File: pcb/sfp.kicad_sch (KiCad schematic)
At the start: 5 parts, among them J1 SFP, U1 GW1N-6&9_QN48

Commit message: pcb: schemat rev. A
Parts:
- added C10, C12, C8: 100n, Capacitor_SMD:C_0603_1608Metric, symbol Device:C
- added C11, C9: 10u, Capacitor_SMD:C_0603_1608Metric, symbol Device:C
- added D2, D3: LED, LED_SMD:LED_0603_1608Metric, symbol Device:LED
- added L1, L2: 1uH, Inductor_SMD:L_0805_2012Metric, symbol Device:L
- added R10, R9: 49.9 1%, Resistor_SMD:R_0402_1005Metric, symbol Device:R
- added R11: 2.1k, Resistor_SMD:R_0603_1608Metric, symbol Device:R
- added R12: 1.2k, Resistor_SMD:R_0603_1608Metric, symbol Device:R
- added R14, R15: 1k, Resistor_SMD:R_0603_1608Metric, symbol Device:R
- added Y1: OT322525MJBA4SL, Oscillator:Oscillator_SMD_Abracon_ASE-4Pin_3.2x2.5mm, symbol Oscillator:ASE-xxxMHz
- C6, C7: footprint Capacitor_SMD:C_0402_1005Metric -> Capacitor_SMD:C_0603_1608Metric
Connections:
- net RD+ is gone; now on net SFP_RD_P: J1.13 (RD+)
- net RD- is gone; now on net SFP_RD_N: J1.12 (RD-)
- net TD+ is gone; now on net SFP_TD_P: J1.18 (TD+)
- net TD- is gone; now on net SFP_TD_N: J1.19 (TD-)
- net CLK_25M: now also Y1.3 (OUT)
- net GND: now also C6.2, C7.2, C10.2, C11.2, C12.2, C8.2, C9.2, R12.2, Y1.2 (GND)
- net LED_ACT: now also D3.1 (K)
- net LED_LINK: now also D2.1 (K)
- net SFP_LOS: now also J1.8 (RX_LOS)
- net SFP_MOD_ABS: now also J1.6 (MOD_DEF0)
- net SFP_RD_N: now also R10.2
- net SFP_RD_P: now also R9.1
- net SFP_TX_DIS: now also J1.3 (TX_DISABLE)
- net SFP_TX_FAULT: now also J1.2 (TX_FAULT)
- net Vbias: now reaches C6.1
- net Vbias: now also R10.1, R11.2, R12.1, R9.2
- net at C7.1: now also J1.16 (VccT), L1.1
- net at J1.15 (VccR): now also C8.1, C9.1, L2.1
- net SFP_SDA: now reaches J1.4 (MOD_DEF2)
- net SFP_SCL: now reaches J1.5 (MOD_DEF1)
- new net: D3.2 (A), R15.2
- new net: D2.2 (A), R14.2
- new net +3V3: C10.1, C11.1, C12.1, L1.2, L2.2, R11.1, R14.1, R15.1, Y1.1 (EN), Y1.4 (Vdd)
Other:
- moved on the sheet: J1, R8, U1A, U1B

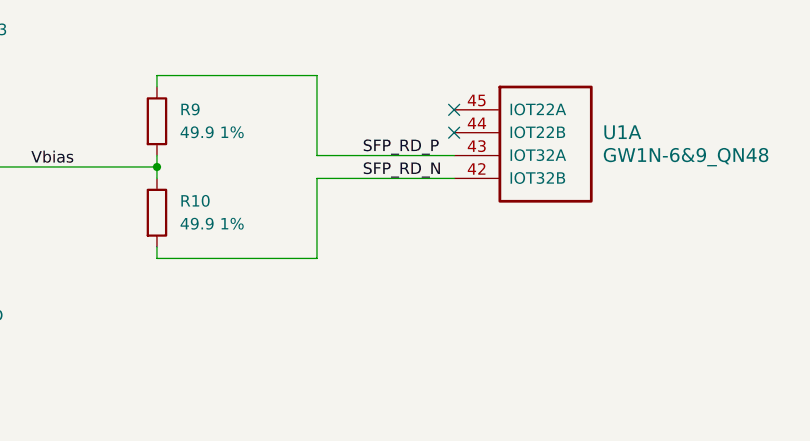
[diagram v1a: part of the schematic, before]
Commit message: pcb: rozmieszczenie i czesc routingu, odwrocona para RD, reguly i klasy sieci
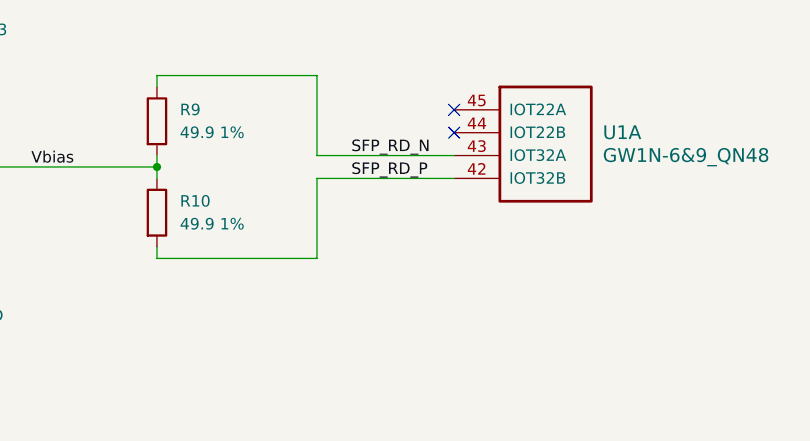
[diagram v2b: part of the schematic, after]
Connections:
- net SFP_RD_N: now also R9.1, U1.43 (IOT32A); no longer R10.2, U1.42 (IOT32B)
- net SFP_RD_P: now also R10.2, U1.42 (IOT32B); no longer R9.1, U1.43 (IOT32A)
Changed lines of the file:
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@@
+		)
+	)
+	(label "SFP_RD_P"
+		(at 220.98 46.99 0)
+		(effects
+			(font
+				(size 1.27 1.27)
+			)
+			(justify left bottom)
 		)
 	)
@@
 		)
 	)
-	(label "SFP_RD_P"
-		(at 222.25 44.45 0)
-		(effects
-			(font
-				(size 1.27 1.27)
-			)
-			(justify left bottom)
-		)
-	)
 	(label "SFP_LOS"
 		(at 201.93 127 0)
@@
 			)
 			(justify right bottom)
+		)
+	)
+	(label "SFP_RD_N"
+		(at 220.98 44.45 0)
+		(effects
+			(font
+				(size 1.27 1.27)
+			)
+			(justify left bottom)
 		)
 	)
@@
 		(effects
 			(font
-				(size 1.27 1.27)
-			)
-			(justify left bottom)
-		)
-	)
-	(label "SFP_RD_N"
-		(at 222.25 46.99 0)
-		(effects
-			(font

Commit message: pcb: routing par LVDS, zasilania i magistrali xSPI
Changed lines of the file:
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@@
 		(fields_autoplaced yes)
 		(property "Reference" "U1"
-			(at 245.11 115.5699 0)
+			(at 240.03 105.4099 0)
 			(show_name no)
 			(do_not_autoplace no)
@@
 		)
 		(property "Value" "GW1N-6&9_QN48"
-			(at 245.11 118.1099 0)
+			(at 240.03 107.9499 0)
 			(show_name no)
 			(do_not_autoplace no)
@@
 		(pin "37"
 		)
+		(pin "49"
+		)
 		(instances
 			(project "SFP_xSPI_Bridge"
+				(path "/ca6491fd-e294-4986-aca7-b24059be2f57/7eb2e6d1-c37f-42de-89f7-3b01f01576cd"
+					(reference "U1")
+					(unit 2)
+				)
 				(path "/ca6491fd-e294-4986-aca7-b24059be2f57/99b2d538-1c3c-4904-a097-9a86c52ff40c"
 					(reference "U1")
@@
 		(fields_autoplaced yes)
 		(property "Reference" "U1"
-			(at 248.92 41.9099 0)
+			(at 256.54 43.1799 0)
 			(show_name no)
 			(do_not_autoplace no)
@@
 		)
 		(property "Value" "GW1N-6&9_QN48"
-			(at 248.92 44.4499 0)
+			(at 256.54 45.7199 0)
 			(show_name no)
 			(do_not_autoplace no)
@@
 		(pin "37"
 		)
+		(pin "49"
+		)
 		(instances
 			(project "SFP_xSPI_Bridge"
+				(path "/ca6491fd-e294-4986-aca7-b24059be2f57/7eb2e6d1-c37f-42de-89f7-3b01f01576cd"
+					(reference "U1")
+					(unit 1)
+				)
 				(path "/ca6491fd-e294-4986-aca7-b24059be2f57/99b2d538-1c3c-4904-a097-9a86c52ff40c"
 					(reference "U1")

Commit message: pcb: rev. A - obrys, strefy, pull-up SFP_TX_DIS, via stitching, usuniete puste arkusze; pliki produkcyjne: gerbery (zip), PDF schematu i PCB, iBOM, rendery 3D
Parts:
- added R17: 4.7k, Resistor_SMD:R_0603_1608Metric, symbol Device:R
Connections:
- net +3V3: now also R17.1
- net SFP_TX_DIS: now also R17.2
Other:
- company: (none) -> bartkepl
- title: (none) -> SFP_xSPI_Bridge
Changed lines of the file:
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@@
 	(generator_version "10.0")
 	(paper "A4")
+	(title_block
+		(title "SFP_xSPI_Bridge")
+		(date "2026-10-09")
+		(rev "A")
+		(company "bartkepl")
+	)
 	(junction
 		(at 95.25 38.1)
@@
 	(wire
 		(pts
+			(xy 193.04 118.11) (xy 193.04 120.65)
+		)
+		(stroke
+			(width 0)
+			(type default)
+		)
+	)
+	(wire
+		(pts
 			(xy 180.34 44.45) (xy 180.34 45.72)
 		)
@@
 	(wire
 		(pts
+			(xy 193.04 132.08) (xy 215.9 132.08)
+		)
+		(stroke
+			(width 0)
+			(type default)
+		)
+	)
+	(wire
+		(pts
 			(xy 140.97 173.99) (xy 140.97 175.26)
 		)
@@
 	(wire
 		(pts
-			(xy 199.39 44.45) (xy 199.39 45.72)
+			(xy 193.04 128.27) (xy 193.04 132.08)
 		)
 		(stroke
@@
 	(wire
 		(pts
-			(xy 95.25 35.56) (xy 95.25 38.1)
+			(xy 199.39 44.45) (xy 199.39 45.72)
 		)
 		(stroke
@@
 	(wire
 		(pts
-			(xy 118.11 66.04) (xy 118.11 68.58)
+			(xy 95.25 35.56) (xy 95.25 38.1)
 		)
 		(stroke
@@
 	(wire
 		(pts
-			(xy 91.44 86.36) (xy 104.14 86.36)
+			(xy 118.11 66.04) (xy 118.11 68.58)
 		)
 		(stroke
@@
 	(wire
 		(pts
-			(xy 176.53 83.82) (xy 176.53 86.36)
+			(xy 91.44 86.36) (xy 104.14 86.36)
 		)
 		(stroke
@@
 	(wire
 		(pts
-			(xy 201.93 132.08) (xy 215.9 132.08)
+			(xy 176.53 83.82) (xy 176.53 86.36)
 		)
 		(stroke
@@
 	)
 	(symbol
+		(lib_id "Device:R")
+		(at 193.04 124.46 0)
+		(unit 1)
+		(body_style 1)
+		(exclude_from_sim no)
+		(in_bom yes)
+		(on_board yes)
+		(in_pos_files yes)
+		(dnp no)
+		(fields_autoplaced yes)
+		(property "Reference" "R17"
+			(at 195.58 123.1899 0)
+			(show_name no)
+			(do_not_autoplace no)
+			(effects
+				(font
+					(size 1.27 1.27)
+				)
+				(justify left)
+			)
+		)
+		(property "Value" "4.7k"
+			(at 195.58 125.7299 0)
+			(show_name no)
+			(do_not_autoplace no)
+			(effects
+				(font
+					(size 1.27 1.27)
+				)
+				(justify left)
+			)
+		)
+		(property "Footprint" "Resistor_SMD:R_0603_1608Metric"
+			(at 191.262 124.46 90)
+			(hide yes)
+			(show_name no)
+			(do_not_autoplace no)
+			(effects
+				(font
+					(size 1.27 1.27)
+				)
+			)
+		)
+		(property "Datasheet" ""
+			(at 193.04 124.46 0)
+			(hide yes)
+			(show_name no)
+			(do_not_autoplace no)
+			(effects
+				(font
+					(size 1.27 1.27)
+				)
+			)
+		)
+		(property "Description" "Resistor"
+			(at 193.04 124.46 0)
+			(hide yes)
+			(show_name no)
+			(do_not_autoplace no)
+			(effects
+				(font
+					(size 1.27 1.27)
+				)
+			)
+		)
+		(property "MF" ""
+			(at 193.04 124.46 0)
+			(hide yes)
+			(show_name no)
+			(do_not_autoplace no)
+			(effects
+				(font
+					(size 1.27 1.27)
+				)
+			)
+		)
+		(property "MPN" ""
+			(at 193.04 124.46 0)
+			(hide yes)
+			(show_name no)
+			(do_not_autoplace no)
+			(effects
+				(font
+					(size 1.27 1.27)
+				)
+			)
+		)
+		(property "PARTNO" ""
+			(at 193.04 124.46 0)
+			(hide yes)
+			(show_name no)
+			(do_not_autoplace no)
+			(effects
+				(font
+					(size 1.27 1.27)
+				)
+			)
+		)
+		(property "LCSC" ""
+			(at 193.04 124.46 0)
+			(hide yes)
+			(show_name no)
+			(do_not_autoplace no)
+			(effects
+				(font
+					(size 1.27 1.27)
+				)
+			)
+		)
+		(pin "1"
+		)
+		(pin "2"
+		)
+		(instances
+			(project "SFP_xSPI_Bridge"
+				(path "/ca6491fd-e294-4986-aca7-b24059be2f57/99b2d538-1c3c-4904-a097-9a86c52ff40c"
+					(reference "R17")
+					(unit 1)
+				)
+			)
+		)
+	)
+	(symbol
 		(lib_id "power:PWR_FLAG")
 		(at 95.25 54.61 0)
@@
 					(unit 1)
 				)
+			)
+		)
+	)
+	(symbol
+		(lib_id "power:+3V3")
+		(at 193.04 118.11 0)
+		(unit 1)
+		(body_style 1)
+		(exclude_from_sim no)
+		(in_bom yes)
+		(on_board yes)
+		(in_pos_files yes)
+		(dnp no)
+		(fields_autoplaced yes)
+		(property "Reference" "#PWR023"
+			(at 193.04 121.92 0)
+			(hide yes)
+			(show_name no)
+			(do_not_autoplace no)
+			(effects
+				(font
+					(size 1.27 1.27)
+				)
+			)
+		)
+		(property "Value" "+3V3"
+			(at 193.04 113.03 0)
+			(show_name no)
+			(do_not_autoplace no)
+			(effects
+				(font
+					(size 1.27 1.27)
+				)
+			)
+		)
+		(property "Footprint" ""
+			(at 193.04 118.11 0)
+			(hide yes)
+			(show_name no)
+			(do_not_autoplace no)
+			(effects
+				(font
+					(size 1.27 1.27)
+				)
+			)
+		)
+		(property "Datasheet" ""
+			(at 193.04 118.11 0)
+			(hide yes)
+			(show_name no)
+			(do_not_autoplace no)
+			(effects
+				(font
+					(size 1.27 1.27)
+				)
+			)
+		)
+		(property "Description" "Power symbol creates a global label with name \"+3V3\""
+			(at 193.04 118.11 0)
+			(hide yes)
+			(show_name no)
+			(do_not_autoplace no)
+			(effects
+				(font
+					(size 1.27 1.27)
+				)
+			)
+		)
+		(pin "1"
+		)
+		(instances
+			(project "SFP_xSPI_Bridge"
+				(path "/ca6491fd-e294-4986-aca7-b24059be2f57/99b2d538-1c3c-4904-a097-9a86c52ff40c"
+					(reference "#PWR023")
+					(unit 1)
+				)
